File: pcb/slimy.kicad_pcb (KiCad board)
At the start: 2 copper layers, 266.7 x 95.2 mm, 99 parts, among them K1 KEYSW, K10 KEYSW, K11 KEYSW, K12 KEYSW, K13 KEYSW, K14 KEYSW, K15 KEYSW, K16 KEYSW, K17 KEYSW, K18 KEYSW, K19 KEYSW, K2 KEYSW, K20 KEYSW, K21 KEYSW, K22 KEYSW, K23 KEYSW, K24 KEYSW, K25 KEYSW, K26 KEYSW, K27 KEYSW, K28 KEYSW, K29 KEYSW, K3 KEYSW, K30 KEYSW, K31 KEYSW, K32 KEYSW, K33 KEYSW, K34 KEYSW, K35 KEYSW, K36 KEYSW, K37 KEYSW, K38 KEYSW, K39 KEYSW, K4 KEYSW, K40 KEYSW, K41 KEYSW, K42 KEYSW, K43 KEYSW, K44 KEYSW, K45 KEYSW, K46 KEYSW, K47 KEYSW, K48 KEYSW, K5 KEYSW, K6 KEYSW, K7 KEYSW, K8 KEYSW, K9 KEYSW, U1 Teensy3.2, U2 ST7789_SPI, U3 PIM447

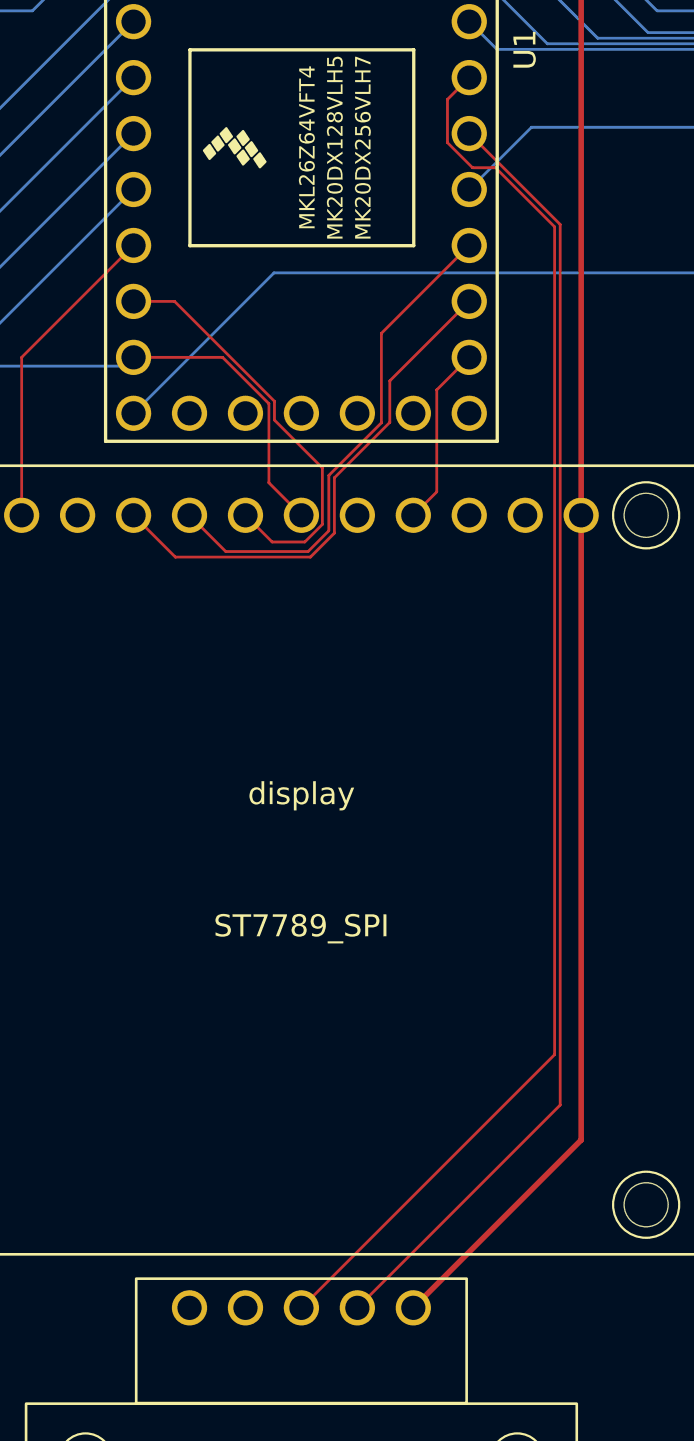
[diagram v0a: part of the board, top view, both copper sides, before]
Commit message: Fix issues with updated pins
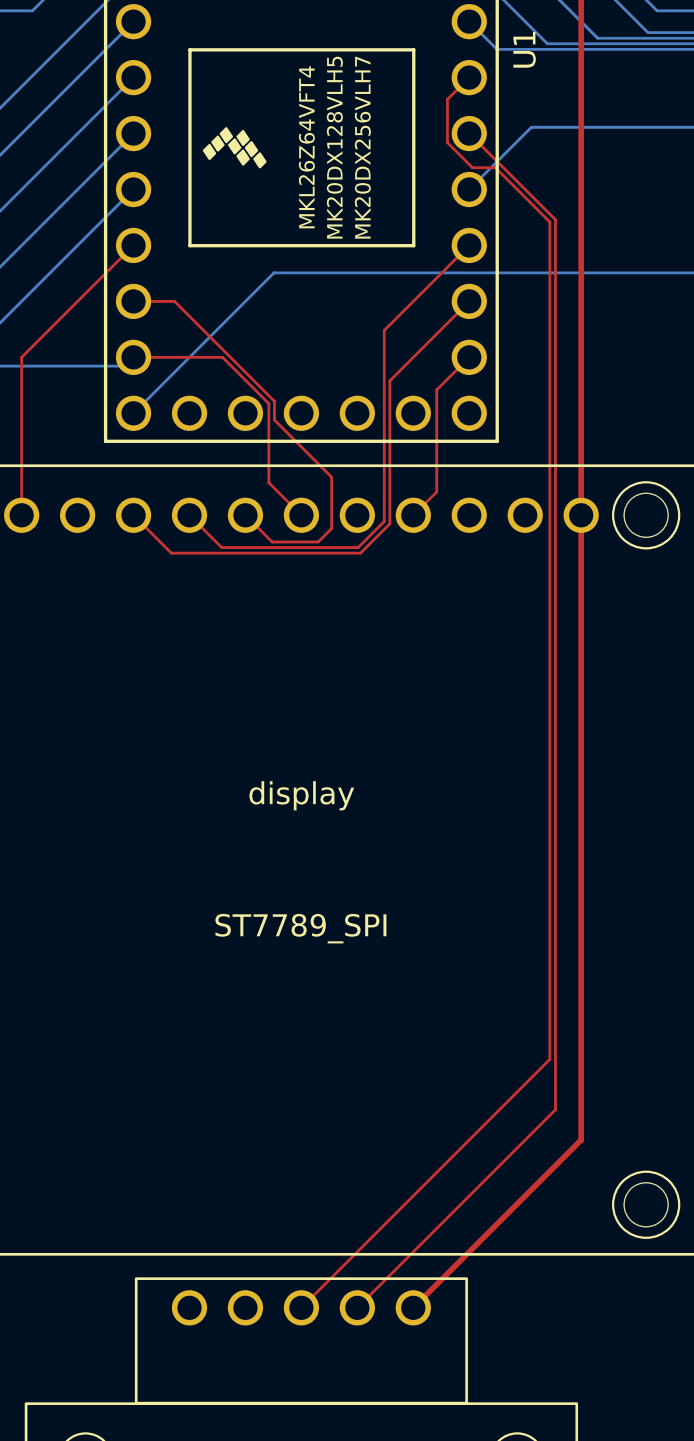
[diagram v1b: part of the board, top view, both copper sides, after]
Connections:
- net Row5 renamed SCK
- U1 pad 29: (no net) -> Col11
- U1 pad 30: (no net) -> Col12
- U1 pad 31: (no net) -> unconnected-(U1-Pad31)
- U1 pad 32: (no net) -> unconnected-(U1-Pad32)
- U1 pad 33: (no net) -> VCC
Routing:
- net LCD RST: track 23.0 -> 24.1 mm
- net LCD DC: track 23.4 -> 24.5 mm
- net LCD CS: track 19.1 -> 19.8 mm

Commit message: Update diode footprint
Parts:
- D1, D10, D11, D12, D13, D14, D15, D16, D17, D18, D19, D2, D20, D21, D22, D23, D24, D25, D26, D27, D28, D29, D3, D30, D31, D32, D33, D34, D35, D36, D37, D38, D39, D4, D40, D41, D42, D43, D44, D45, D46, D47, D48, D5, D6, D7, D8, D9: footprint my_lib:D_SOD123_axial -> my_lib:1N4148
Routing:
- net Net-(D20-Pad2): track 79.1 -> 80.9 mm
- net Net-(D16-Pad2): track 79.1 -> 80.9 mm
- net Net-(D8-Pad2): track 79.1 -> 80.9 mm
- net Net-(D4-Pad2): track 79.1 -> 80.9 mm
- net Net-(D12-Pad2): track 79.1 -> 80.9 mm
- net Net-(D15-Pad2): track 56.8 -> 58.6 mm
- net Net-(D7-Pad2): track 56.8 -> 58.6 mm
- net Net-(D3-Pad2): track 56.8 -> 58.6 mm
- net Net-(D19-Pad2): track 56.8 -> 58.6 mm
- net Net-(D11-Pad2): track 56.8 -> 58.6 mm
- net Net-(D24-Pad2): track 79.1 -> 80.9 mm
- net Net-(D9-Pad2): track 13.5 -> 15.2 mm
- net Net-(D5-Pad2): track 13.5 -> 15.2 mm
- net Net-(D1-Pad2): track 13.5 -> 15.2 mm
- net Net-(D17-Pad2): track 13.5 -> 15.2 mm
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
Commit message: Round PBC corners
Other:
- board size 266.7 x 95.2 mm -> 266.7 x 95.3 mm
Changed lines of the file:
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@@
       (net 36 "Net-(D32-Pad2)") (pintype "passive"))
   )
-  (gr_rect (start 82.3468 183.5404) (end 349.0468 88.2904) (layer "Edge.Cuts") (width 0.1) (fill none))
+  (gr_line (start 82.336818 89.169418) (end 82.3468 182.6514) (layer "Edge.Cuts") (width 0.1))
+  (gr_arc (start 348.167706 88.280418) (mid 348.796324 88.5408) (end 349.056706 89.169418) (layer "Edge.Cuts") (width 0.1))
+  (gr_line (start 349.056706 89.169418) (end 349.056706 182.661382) (layer "Edge.Cuts") (width 0.1))
+  (gr_line (start 348.167706 183.550382) (end 83.2358 183.5404) (layer "Edge.Cuts") (width 0.1))
+  (gr_line (start 348.167706 88.280418) (end 83.225818 88.280418) (layer "Edge.Cuts") (width 0.1))
+  (gr_arc (start 349.056706 182.661382) (mid 348.796324 183.29) (end 348.167706 183.550382) (layer "Edge.Cuts") (width 0.1))
+  (gr_arc (start 83.2358 183.5404) (mid 82.607182 183.280018) (end 82.3468 182.6514) (layer "Edge.Cuts") (width 0.1))
+  (gr_arc (start 82.336818 89.169418) (mid 82.5972 88.5408) (end 83.225818 88.280418) (layer "Edge.Cuts") (width 0.1))
   (segment (start 188.4156 103.24084) (end 189.5078 104.33304) (width 0.127) (layer "B.Cu") (net 1))
   (segment (start 278.9158 103.24084) (end 262.0248 103.24084) (width 0.127) (layer "B.Cu") (net 1))
@@
   (segment (start 330.6302 153.1874) (end 330.6302 170.7134) (width 0.127) (layer "F.Cu") (net 64))
   (segment (start 330.6302 134.1374) (end 330.6302 151.6634) (width 0.127) (layer "F.Cu") (net 64))
-  (segment (start 231.52084 105.38604) (end 223.3152 97.1804) (width 0.127) (layer "B.Cu") (net 64))
-  (segment (start 330.6302 112.223378) (end 323.792862 105.38604) (width 0.127) (layer "B.Cu") (net 64))
-  (segment (start 323.792862 105.38604) (end 231.52084 105.38604) (width 0.127) (layer "B.Cu") (net 64))
+  (segment (start 231.432451 105.297651) (end 223.3152 97.1804) (width 0.127) (layer "B.Cu") (net 64))
+  (segment (start 323.704473 105.297651) (end 231.432451 105.297651) (width 0.127) (layer "B.Cu") (net 64))
+  (segment (start 330.6302 112.223378) (end 323.704473 105.297651) (width 0.127) (layer "B.Cu") (net 64))
   (segment (start 330.6302 113.5634) (end 330.6302 112.223378) (width 0.127) (layer "B.Cu") (net 64))
   (segment (start 221.838211 121.517389) (end 223.3152 120.0404) (width 0.127) (layer "F.Cu") (net 71))

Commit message: Add logo
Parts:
- added G***: LOGO, slimy_footprints:slimy-logo, B.Cu at (215.8, 144.1)

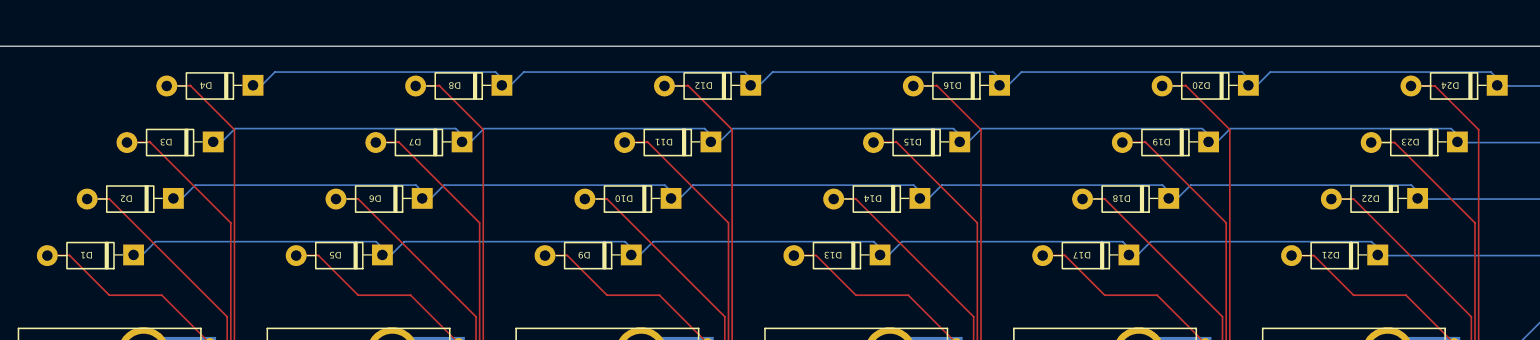
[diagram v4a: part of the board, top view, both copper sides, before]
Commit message: Update diode footprint
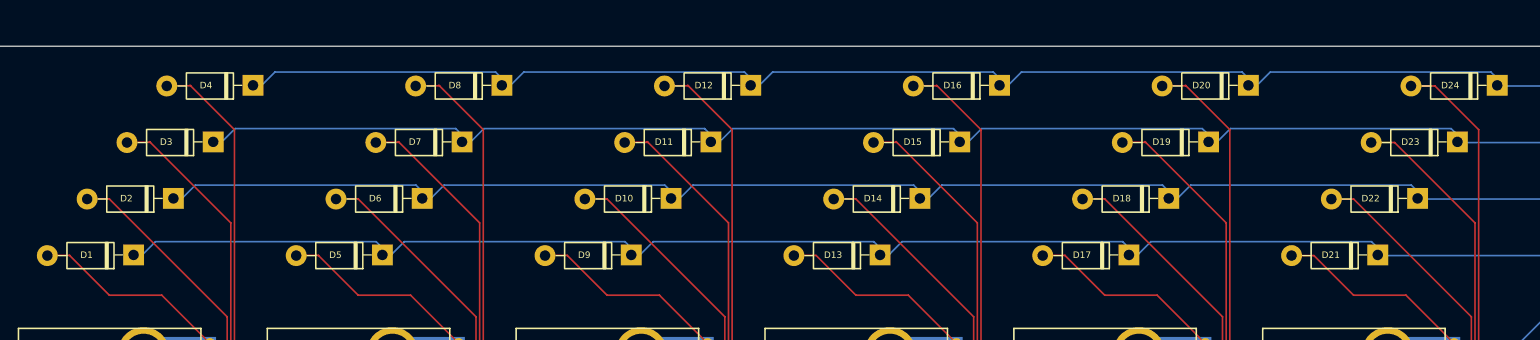
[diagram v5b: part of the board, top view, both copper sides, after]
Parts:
- D1, D10, D11, D12, D13, D14, D15, D16, D17, D18, D19, D2, D20, D21, D22, D23, D24, D25, D26, D27, D28, D29, D3, D30, D31, D32, D33, D34, D35, D36, D37, D38, D39, D4, D40, D41, D42, D43, D44, D45, D46, D47, D48, D5, D6, D7, D8, D9: footprint my_lib:1N4148 -> my_lib:D_1N4148
